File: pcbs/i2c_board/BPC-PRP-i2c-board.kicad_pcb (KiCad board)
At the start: 2 copper layers, 60 x 60 mm, 16 parts, among them J1 Power, J2 I2C, J3 I2C_Aux, J4 ADC, J5 I2C_Aux

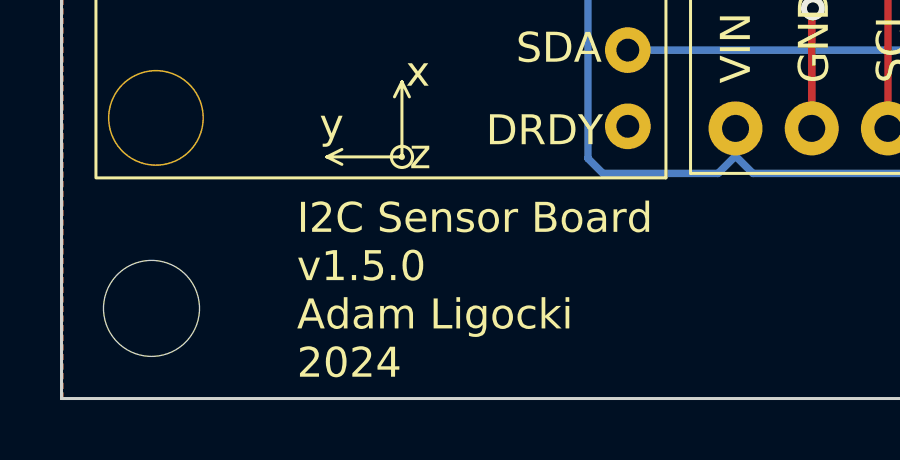
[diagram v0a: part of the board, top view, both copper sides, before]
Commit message: minor update i2c board, added pdbs schematics and renders
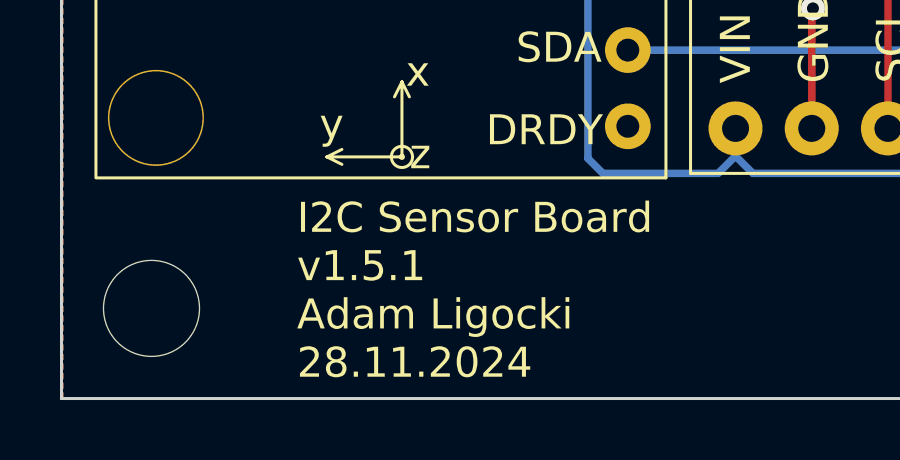
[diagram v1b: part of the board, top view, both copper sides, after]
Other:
- board text added: "I2C Sensor Board v1.5.1 Adam Ligocki 28.11.2024"
- board text removed: "I2C Sensor Board v1.5.0 Adam Ligocki 2024"
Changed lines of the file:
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@@
 		)
 	)
-	(gr_text "I2C Sensor Board\nv1.5.0\nAdam Ligocki\n2024\n"
+	(gr_text "I2C Sensor Board\nv1.5.1\nAdam Ligocki\n28.11.2024\n"
 		(at 127.8 129.4 0)
 		(layer "F.SilkS")

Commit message: add i2c pullups for rpi ext and i2c board
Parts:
- added R2: 2k2, Resistor_SMD:R_1206_3216Metric, F.Cu at (145.7, 84.4)
- added R3: 2k2, Resistor_SMD:R_1206_3216Metric, F.Cu at (145.7, 86.8)
- R1: value R -> 10k
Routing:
- net SDA: track 147.5 -> 162.4 mm, vias 0 -> 1
- net VCC: track 192.7 -> 204.0 mm
- net SCL: track 149.6 -> 159.3 mm
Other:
- board text added: "I2C Sensor Board v1.5.2 Adam Ligocki 01.12.2024"
- board text removed: "I2C Sensor Board v1.5.1 Adam Ligocki 28.11.2024"
